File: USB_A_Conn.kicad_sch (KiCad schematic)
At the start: 5 parts, among them J7 USB_A_Stacked, U14 USBLC6-2SC6, U15 USBLC6-2SC6

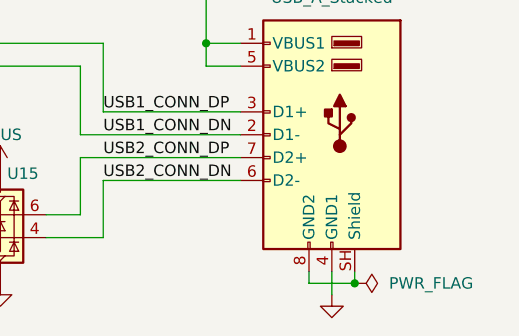
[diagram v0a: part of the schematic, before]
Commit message: VBUS and +3V3 zones routing
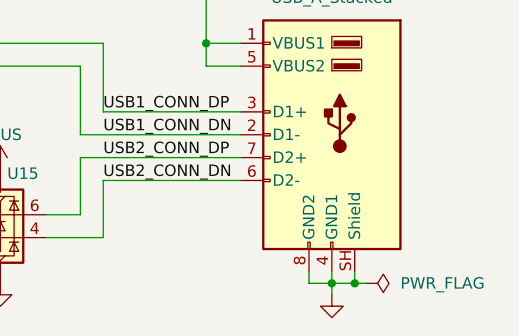
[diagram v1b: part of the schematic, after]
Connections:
- net GND: now also J7.8 (GND2), J7.SH (Shield)
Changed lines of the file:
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@@
+	)
+	(junction
+		(at 156.21 116.84)
+		(diameter 0)
+		(color 0 0 0 0)
 	)
 	(junction
@@
 	)
 	(junction
-		(at 156.21 116.84)
+		(at 153.67 116.84)
 		(diameter 0)
 		(color 0 0 0 0)
@@
 	(wire
 		(pts
-			(xy 151.13 116.84) (xy 156.21 116.84)
+			(xy 153.67 116.84) (xy 153.67 118.11)
+		)
+		(stroke
+			(width 0)
+			(type default)
+		)
+	)
+	(wire
+		(pts
+			(xy 153.67 116.84) (xy 156.21 116.84)
 		)
 		(stroke
@@
 	(wire
 		(pts
-			(xy 153.67 115.57) (xy 153.67 118.11)
+			(xy 153.67 115.57) (xy 153.67 116.84)
+		)
+		(stroke
+			(width 0)
+			(type default)
+		)
+	)
+	(wire
+		(pts
+			(xy 157.48 116.84) (xy 156.21 116.84)
+		)
+		(stroke
+			(width 0)
+			(type default)
+		)
+	)
+	(wire
+		(pts
+			(xy 151.13 116.84) (xy 153.67 116.84)
 		)
 		(stroke
@@
 	(symbol
 		(lib_id "power:PWR_FLAG")
-		(at 156.21 116.84 270)
+		(at 157.48 116.84 270)
 		(unit 1)
 		(body_style 1)
@@
 		(fields_autoplaced yes)
 		(property "Reference" "#FLG05"
-			(at 158.115 116.84 0)
+			(at 159.385 116.84 0)
 			(hide yes)
 			(show_name no)
@@
 		)
 		(property "Value" "PWR_FLAG"
-			(at 160.02 116.8399 90)
+			(at 161.29 116.8399 90)
 			(show_name no)
 			(do_not_autoplace no)
@@
 		)
 		(property "Footprint" ""
-			(at 156.21 116.84 0)
+			(at 157.48 116.84 0)
 			(hide yes)
 			(show_name no)
@@
 		)
 		(property "Datasheet" ""
-			(at 156.21 116.84 0)
+			(at 157.48 116.84 0)
 			(hide yes)
 			(show_name no)
@@
 		)
 		(property "Description" "Special symbol for telling ERC where power comes from"
-			(at 156.21 116.84 0)
-			(hide yes)
-			(show_name no)
+			(at 157.48 116.84 0)
+			(hide yes)
+			(show_name no)

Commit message: Added ESD protection for the remaining HDMI pins - Not routed yet
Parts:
- renumbered U14 to U17, U15 to U18
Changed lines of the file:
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@@
 		(in_pos_files yes)
 		(dnp no)
-		(property "Reference" "U15"
+		(property "Reference" "U18"
 			(at 117.602 104.648 0)
 			(show_name no)
@@
 			(project "KVM_Switch"
 				(path "/94386106-ccd4-487f-b5c5-d52ec3dd59db/0e1d684f-830c-4bab-be20-dfd6c92d7874/9225d246-3ad2-4927-a45b-bd5165c1e795"
-					(reference "U17")
-					(unit 1)
-				)
-				(path "/94386106-ccd4-487f-b5c5-d52ec3dd59db/0e1d684f-830c-4bab-be20-dfd6c92d7874/b872fb37-3607-4e08-a4aa-9f2b2b22c725"
-					(reference "U15")
+					(reference "U20")
+					(unit 1)
+				)
+				(path "/94386106-ccd4-487f-b5c5-d52ec3dd59db/0e1d684f-830c-4bab-be20-dfd6c92d7874/b872fb37-3607-4e08-a4aa-9f2b2b22c725"
+					(reference "U18")
 					(unit 1)
 				)
@@
 		(dnp no)
 		(fields_autoplaced yes)
-		(property "Reference" "#PWR064"
+		(property "Reference" "#PWR070"
 			(at 153.67 124.46 0)
 			(hide yes)
@@
 			(project "KVM_Switch"
 				(path "/94386106-ccd4-487f-b5c5-d52ec3dd59db/0e1d684f-830c-4bab-be20-dfd6c92d7874/9225d246-3ad2-4927-a45b-bd5165c1e795"
-					(reference "#PWR071")
-					(unit 1)
-				)
-				(path "/94386106-ccd4-487f-b5c5-d52ec3dd59db/0e1d684f-830c-4bab-be20-dfd6c92d7874/b872fb37-3607-4e08-a4aa-9f2b2b22c725"
-					(reference "#PWR064")
+					(reference "#PWR077")
+					(unit 1)
+				)
+				(path "/94386106-ccd4-487f-b5c5-d52ec3dd59db/0e1d684f-830c-4bab-be20-dfd6c92d7874/b872fb37-3607-4e08-a4aa-9f2b2b22c725"
+					(reference "#PWR070")
 					(unit 1)
 				)
@@
 		(in_pos_files yes)
 		(dnp no)
-		(property "Reference" "#PWR062"
+		(property "Reference" "#PWR068"
 			(at 116.84 107.95 0)
 			(hide yes)
@@
 			(project "KVM_Switch"
 				(path "/94386106-ccd4-487f-b5c5-d52ec3dd59db/0e1d684f-830c-4bab-be20-dfd6c92d7874/9225d246-3ad2-4927-a45b-bd5165c1e795"
-					(reference "#PWR069")
-					(unit 1)
-				)
-				(path "/94386106-ccd4-487f-b5c5-d52ec3dd59db/0e1d684f-830c-4bab-be20-dfd6c92d7874/b872fb37-3607-4e08-a4aa-9f2b2b22c725"
-					(reference "#PWR062")
+					(reference "#PWR075")
+					(unit 1)
+				)
+				(path "/94386106-ccd4-487f-b5c5-d52ec3dd59db/0e1d684f-830c-4bab-be20-dfd6c92d7874/b872fb37-3607-4e08-a4aa-9f2b2b22c725"
+					(reference "#PWR068")
 					(unit 1)
 				)
@@
 		(dnp no)
 		(fields_autoplaced yes)
-		(property "Reference" "#PWR061"
+		(property "Reference" "#PWR067"
 			(at 109.22 104.14 0)
 			(hide yes)
@@
 			(project "KVM_Switch"
 				(path "/94386106-ccd4-487f-b5c5-d52ec3dd59db/0e1d684f-830c-4bab-be20-dfd6c92d7874/9225d246-3ad2-4927-a45b-bd5165c1e795"
-					(reference "#PWR068")
-					(unit 1)
-				)
-				(path "/94386106-ccd4-487f-b5c5-d52ec3dd59db/0e1d684f-830c-4bab-be20-dfd6c92d7874/b872fb37-3607-4e08-a4aa-9f2b2b22c725"
-					(reference "#PWR061")
+					(reference "#PWR074")
+					(unit 1)
+				)
+				(path "/94386106-ccd4-487f-b5c5-d52ec3dd59db/0e1d684f-830c-4bab-be20-dfd6c92d7874/b872fb37-3607-4e08-a4aa-9f2b2b22c725"
+					(reference "#PWR067")
 					(unit 1)
 				)
@@
 		(dnp no)
 		(fields_autoplaced yes)
-		(property "Reference" "#PWR063"
+		(property "Reference" "#PWR069"
 			(at 116.84 123.19 0)
 			(hide yes)
@@
 			(project "KVM_Switch"
 				(path "/94386106-ccd4-487f-b5c5-d52ec3dd59db/0e1d684f-830c-4bab-be20-dfd6c92d7874/9225d246-3ad2-4927-a45b-bd5165c1e795"
-					(reference "#PWR070")
-					(unit 1)
-				)
-				(path "/94386106-ccd4-487f-b5c5-d52ec3dd59db/0e1d684f-830c-4bab-be20-dfd6c92d7874/b872fb37-3607-4e08-a4aa-9f2b2b22c725"
-					(reference "#PWR063")
+					(reference "#PWR076")
+					(unit 1)
+				)
+				(path "/94386106-ccd4-487f-b5c5-d52ec3dd59db/0e1d684f-830c-4bab-be20-dfd6c92d7874/b872fb37-3607-4e08-a4aa-9f2b2b22c725"
+					(reference "#PWR069")
 					(unit 1)
 				)
@@
 		(dnp no)
 		(fields_autoplaced yes)
-		(property "Reference" "#PWR059"
+		(property "Reference" "#PWR065"
 			(at 124.46 85.09 0)
 			(hide yes)
@@
 			(project "KVM_Switch"
 				(path "/94386106-ccd4-487f-b5c5-d52ec3dd59db/0e1d684f-830c-4bab-be20-dfd6c92d7874/9225d246-3ad2-4927-a45b-bd5165c1e795"
-					(reference "#PWR066")
-					(unit 1)
-				)
-				(path "/94386106-ccd4-487f-b5c5-d52ec3dd59db/0e1d684f-830c-4bab-be20-dfd6c92d7874/b872fb37-3607-4e08-a4aa-9f2b2b22c725"
-					(reference "#PWR059")
+					(reference "#PWR072")
+					(unit 1)
+				)
+				(path "/94386106-ccd4-487f-b5c5-d52ec3dd59db/0e1d684f-830c-4bab-be20-dfd6c92d7874/b872fb37-3607-4e08-a4aa-9f2b2b22c725"
+					(reference "#PWR065")
 					(unit 1)
 				)
@@
 		(in_pos_files yes)
 		(dnp no)
-		(property "Reference" "U14"
+		(property "Reference" "U17"
 			(at 109.982 85.598 0)
 			(show_name no)
@@
 			(project "KVM_Switch"
 				(path "/94386106-ccd4-487f-b5c5-d52ec3dd59db/0e1d684f-830c-4bab-be20-dfd6c92d7874/9225d246-3ad2-4927-a45b-bd5165c1e795"
-					(reference "U16")
-					(unit 1)
-				)
-				(path "/94386106-ccd4-487f-b5c5-d52ec3dd59db/0e1d684f-830c-4bab-be20-dfd6c92d7874/b872fb37-3607-4e08-a4aa-9f2b2b22c725"
-					(reference "U14")
+					(reference "U19")
+					(unit 1)
+				)
+				(path "/94386106-ccd4-487f-b5c5-d52ec3dd59db/0e1d684f-830c-4bab-be20-dfd6c92d7874/b872fb37-3607-4e08-a4aa-9f2b2b22c725"
+					(reference "U17")
 					(unit 1)
 				)
@@
 		(in_pos_files yes)
 		(dnp no)
-		(property "Reference" "#PWR060"
+		(property "Reference" "#PWR066"
 			(at 109.22 88.9 0)
 			(hide yes)
@@
 			(project "KVM_Switch"
 				(path "/94386106-ccd4-487f-b5c5-d52ec3dd59db/0e1d684f-830c-4bab-be20-dfd6c92d7874/9225d246-3ad2-4927-a45b-bd5165c1e795"
-					(reference "#PWR067")
-					(unit 1)
-				)
-				(path "/94386106-ccd4-487f-b5c5-d52ec3dd59db/0e1d684f-830c-4bab-be20-dfd6c92d7874/b872fb37-3607-4e08-a4aa-9f2b2b22c725"
-					(reference "#PWR060")
+					(reference "#PWR073")
+					(unit 1)
+				)
+				(path "/94386106-ccd4-487f-b5c5-d52ec3dd59db/0e1d684f-830c-4bab-be20-dfd6c92d7874/b872fb37-3607-4e08-a4aa-9f2b2b22c725"
+					(reference "#PWR066")
 					(unit 1)
 				)
@@
 		(in_pos_files yes)
 		(dnp no)
-		(property "Reference" "#PWR058"
+		(property "Reference" "#PWR064"
 			(at 139.7 68.58 0)
 			(hide yes)
@@
 			(project "KVM_Switch"
 				(path "/94386106-ccd4-487f-b5c5-d52ec3dd59db/0e1d684f-830c-4bab-be20-dfd6c92d7874/9225d246-3ad2-4927-a45b-bd5165c1e795"
-					(reference "#PWR065")
-					(unit 1)
-				)
-				(path "/94386106-ccd4-487f-b5c5-d52ec3dd59db/0e1d684f-830c-4bab-be20-dfd6c92d7874/b872fb37-3607-4e08-a4aa-9f2b2b22c725"
-					(reference "#PWR058")
-					(unit 1)
-				)
+					(reference "#PWR071")
+					(unit 1)
+				)
+				(path "/94386106-ccd4-487f-b5c5-d52ec3dd59db/0e1d684f-830c-4bab-be20-dfd6c92d7874/b872fb37-3607-4e08-a4aa-9f2b2b22c725"
+					(reference "#PWR064")
+					(unit 1)
+				)

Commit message: Fix naming typo: KVM_Swtich -> KVM_Switch
Renamed the footprint library folder library/KVM_Swtich.pretty to
library/KVM_Switch.pretty and the 3D model swtich_smd_6x6mm.step to
switch_smd_6x6mm.step, and updated every reference across
fp-lib-table, sym-lib-table, the schematics, symbols.kicad_sym, and
the PCB. Also fixed a stray "Swtich A to C" text label.
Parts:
- J7: footprint KVM_Swtich:USB_A_Wuerth_61400826021_Horizontal_Stacked -> KVM_Switch:USB_A_Wuerth_61400826021_Horizontal_Stacked
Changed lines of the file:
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@@
 			)
 		)
-		(property "Footprint" "KVM_Swtich:USB_A_Wuerth_61400826021_Horizontal_Stacked"
+		(property "Footprint" "KVM_Switch:USB_A_Wuerth_61400826021_Horizontal_Stacked"
 			(at 149.86 114.3 0)
 			(hide yes)

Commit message: Updated custom rules & Changed switch
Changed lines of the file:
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@@
-	)
-	(junction
-		(at 156.21 116.84)
-		(diameter 0)
-		(color 0 0 0 0)
 	)
 	(junction
@@
 		(pts
 			(xy 153.67 115.57) (xy 153.67 116.84)
-		)
-		(stroke
-			(width 0)
-			(type default)
-		)
-	)
-	(wire
-		(pts
-			(xy 157.48 116.84) (xy 156.21 116.84)
 		)
 		(stroke
@@
 					(unit 1)
 				)
-			)
-		)
-	)
-	(symbol
-		(lib_id "power:PWR_FLAG")
-		(at 157.48 116.84 270)
-		(unit 1)
-		(body_style 1)
-		(exclude_from_sim no)
-		(in_bom yes)
-		(on_board yes)
-		(in_pos_files yes)
-		(dnp no)
-		(fields_autoplaced yes)
-		(property "Reference" "#FLG05"
-			(at 159.385 116.84 0)
-			(hide yes)
-			(show_name no)
-			(do_not_autoplace no)
-			(effects
-				(font
-					(size 1.27 1.27)
-				)
-			)
-		)
-		(property "Value" "PWR_FLAG"
-			(at 161.29 116.8399 90)
-			(show_name no)
-			(do_not_autoplace no)
-			(effects
-				(font
-					(size 1.27 1.27)
-				)
-				(justify left)
-			)
-		)
-		(property "Footprint" ""
-			(at 157.48 116.84 0)
-			(hide yes)
-			(show_name no)
-			(do_not_autoplace no)
-			(effects
-				(font
-					(size 1.27 1.27)
-				)
-			)
-		)
-		(property "Datasheet" ""
-			(at 157.48 116.84 0)
-			(hide yes)
-			(show_name no)
-			(do_not_autoplace no)
-			(effects
-				(font
-					(size 1.27 1.27)
-				)
-			)
-		)
-		(property "Description" "Special symbol for telling ERC where power comes from"
-			(at 157.48 116.84 0)
-			(hide yes)
-			(show_name no)
-			(do_not_autoplace no)
-			(effects
-				(font
-					(size 1.27 1.27)
-				)
-			)
-		)
-		(pin "1"
-		)
-		(instances
-			(project "KVM_Switch"
-				(path "/94386106-ccd4-487f-b5c5-d52ec3dd59db/0e1d684f-830c-4bab-be20-dfd6c92d7874/9225d246-3ad2-4927-a45b-bd5165c1e795"
-					(reference "#FLG06")
-					(unit 1)
-				)
-				(path "/94386106-ccd4-487f-b5c5-d52ec3dd59db/0e1d684f-830c-4bab-be20-dfd6c92d7874/b872fb37-3607-4e08-a4aa-9f2b2b22c725"
-					(reference "#FLG05")
-					(unit 1)
-				)
